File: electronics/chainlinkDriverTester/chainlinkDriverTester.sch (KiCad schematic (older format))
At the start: 145 parts, among them J1 Barrel_Jack_Switch, J10 Sensor C, J11 Sensor D, J12 Motor E, J13 Motor F, J14 Sensor E, J15 Sensor F, J2 Conn_01x03_Female, J22 Power, J26 exp, J27 exp, J28 exp, J29 exp, J3 Motor A, J30 exp, J31 exp, J32 Conn_01x06_Female, J5 Motor B, J6 Motor C, J7 Motor D, J8 Sensor A, J9 Sensor B, SW1 SW_Push, U1 AP7361C-33E, U2 TTGO_TDisplay, U3 VN7007ALH, U4 MCP23017_SS, U5 INA219BxD, U7 Buck

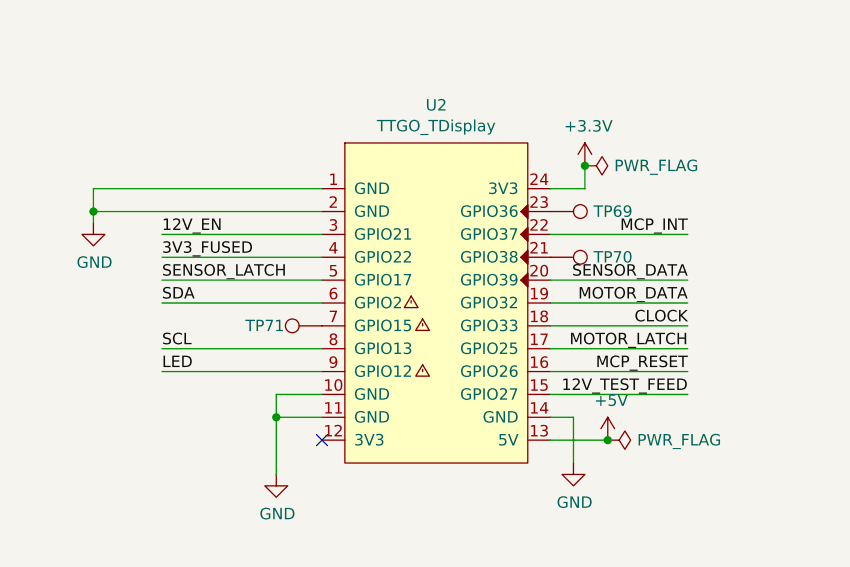
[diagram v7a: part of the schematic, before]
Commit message: Add chainlinkDriverTester firmware, improve chainlink firmware, fix PCB T-Display pinouts (#172)
- Add chainlinkDriverTester firmware with full test implementation, including barcode serial scanning and publishing results to firestore
- Refactor and clean up chainlink firmware for better multi-task support (queue-based commands)
- Implement iterative loopback testing during normal run loop in chainlink (currently logging failures only; doesn't affect behavior)
- Split platformio builds in GitHub Actions for more granular firmware build results
- Fix bad ESP32 pinout choices in chainlinkDriverTester PCB/schematic
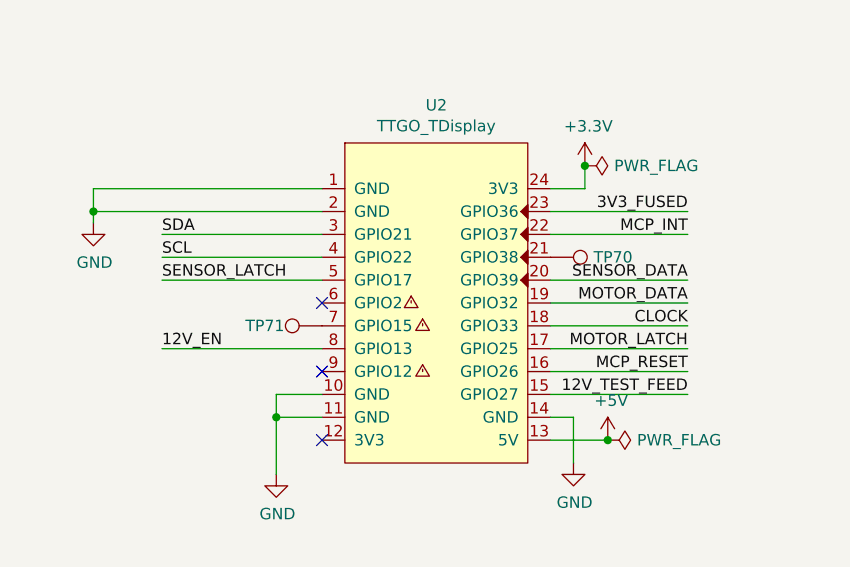
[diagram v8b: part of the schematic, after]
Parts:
- removed TP69: TestPoint, TestPoint:TestPoint_THTPad_D2.0mm_Drill1.0mm, symbol Connector:TestPoint
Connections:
- net 12V_EN: now also U2.8 (GPIO13); no longer U2.3 (GPIO21)
- net 3V3_FUSED: now also U2.23 (GPIO36); no longer U2.4 (GPIO22)
- net SCL: now also U2.4 (GPIO22); no longer U2.8 (GPIO13)
- net SDA: now also U2.3 (GPIO21); no longer U2.6 (GPIO2)
- net LED: no longer names the net of U2.9 (GPIO12)
- no-connect marks 18 -> 20
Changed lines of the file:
@@
 Text Label 4200 4500 2    50   ~ 0
 SENSOR_DATA
-Text Label 1900 4600 0    50   ~ 0
+Text Label 1900 4300 0    50   ~ 0
 SDA
-Text Label 1900 4800 0    50   ~ 0
+Text Label 1900 4400 0    50   ~ 0
 SCL
 Wire Wire Line
@@
 	3600 4900 4200 4900
 Wire Wire Line
-	1900 4600 2600 4600
-Wire Wire Line
-	1900 4800 2600 4800
-Wire Wire Line
-	2600 4300 1900 4300
+	1900 4300 2600 4300
+Wire Wire Line
+	1900 4400 2600 4400
+Wire Wire Line
+	2600 4800 1900 4800
 Text Label 4200 4300 2    50   ~ 0
 MCP_INT
@@
 Wire Wire Line
 	4200 5000 3600 5000
-Text Label 1900 4300 0    50   ~ 0
+Text Label 1900 4800 0    50   ~ 0
 12V_EN
 Wire Wire Line
@@
 Text Label 9800 1100 2    50   ~ 0
 3V3_FUSED
-Text Label 1900 4400 0    50   ~ 0
+Text Label 4200 4200 2    50   ~ 0
 3V3_FUSED
 Text Label 2950 8100 0    50   ~ 0
 3V3_FUSED
 Connection ~ 3650 8100
-Wire Wire Line
-	1900 4400 2600 4400
 $Comp
 L Regulator_Linear:AP7361C-33E U1
@@
 NoConn ~ 15950 1300
 $Comp
-L Connector:TestPoint TP69
-U 1 1 62B86D3D
-P 3600 4200
-F 0 "TP69" V 3600 4388 50  0000 L CNN
-F 1 "TestPoint" V 3645 4388 50  0001 L CNN
-F 2 "TestPoint:TestPoint_THTPad_D2.0mm_Drill1.0mm" H 3800 4200 50  0001 C CNN
-F 3 "~" H 3800 4200 50  0001 C CNN
-	1    3600 4200
-	0    1    1    0
-$EndComp
-$Comp
 L Connector:TestPoint TP70
 U 1 1 62B87233
@@
 	0    -1   -1   0
 $EndComp
-Wire Wire Line
-	1900 4900 2600 4900
-Text Label 1900 4900 0    50   ~ 0
-LED
 NoConn ~ 2600 5200
 Text Label 8800 6600 0    50   ~ 0
@@
 Text Label 9550 6100 2    50   ~ 0
 DETECT
+Wire Wire Line
+	4200 4200 3600 4200
+NoConn ~ 2600 4600
+NoConn ~ 2600 4900
 $EndSCHEMATC
